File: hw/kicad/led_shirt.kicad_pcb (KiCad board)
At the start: 2 copper layers, 20.6 x 20.6 mm, 22 parts, among them J1 10103593-0001LF, P6 b+, P7 b-, Q1 MOS_N_np, SW1 SW_PUSH, U1 MCP73831, U2 PIC12F1822

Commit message: save some changes. need to switch to dual n-fet package.
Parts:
- removed P6: b+, noah_hole_1
- removed P7: b-, noah_hole_1
- removed med_test_hole (x2): VAL**, med_test_hole
- Q1: value MOS_N_np -> MOSFET_N
- R1: value 3.3kΩ -> 10kΩ
- R2: value 3.3kΩ -> 0Ω
- R3: value 10kΩ -> 10K
- R4: value 0Ω -> 10K
- R5, R6: value 10K -> 3.3kΩ
- U1: value MCP73831 -> PIC12F1822
- U2: value PIC12F1822 -> MCP73831
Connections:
- D1 pad 1: vbus -> vbat
- D1 pad 2: N-0000013 -> Net-(D1-Pad2)
- D2 pad 2: N-0000018 -> Net-(D1-Pad2)
- D3 pad 2: N-0000018 -> Net-(D1-Pad2)
- D4 pad 2: N-0000018 -> Net-(D1-Pad2)
- D5 pad 1: vbat -> vbus
- D5 pad 2: N-0000018 -> Net-(D5-Pad2)
- J1 pad 2: (no net) -> icspdat
- J1 pad 3: (no net) -> mclr
- J1 pad 4: (no net) -> icspclk
- Q1 pad 1: N-0000011 -> Net-(Q1-Pad1)
- Q1 pad 2: GND -> Net-(Q1-Pad2)
- Q1 pad 3: N-0000016 -> vbat
- R1 pad 1: N-0000013 -> Net-(Q1-Pad1)
- R1 pad 2: N-000001 -> GND
- R2 pad 1: N-0000014 -> Net-(D1-Pad2)
- R2 pad 2: GND -> Net-(Q2-Pad3)
- R3 pad 1: vbat -> mclr
- R3 pad 2: N-0000017 -> vbat
- R4 pad 1: N-0000018 -> Net-(Q2-Pad1)
- R4 pad 2: N-0000016 -> GND
- R5 pad 1: mclr -> Net-(R5-Pad1)
- R5 pad 2: vbat -> GND
- R6 pad 1: N-0000011 -> Net-(D5-Pad2)
- R6 pad 2: GND -> Net-(R6-Pad2)
- SW1 pad 1: GND -> vbat
- SW1 pad 2: N-0000017 -> Net-(Q1-Pad1)
- U1 pad 1: N-000001 -> Net-(Q1-Pad2)
- U1 pad 2: GND -> Net-(Q1-Pad1)
- U1 pad 3: vbat -> Net-(U1-Pad3)
- U1 pad 4: vbus -> mclr
- U1 pad 5: N-0000014 -> Net-(Q2-Pad1)
- U2 pad 1: vbat -> Net-(R6-Pad2)
- U2 pad 2: N-0000017 -> GND
- U2 pad 3: (no net) -> vbat
- U2 pad 4: mclr -> vbus
- U2 pad 5: N-0000011 -> Net-(R5-Pad1)
- U2 pad 8: GND -> (no net)
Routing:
- net N-0000018: track 35.3 -> 0.00 mm, vias 2 -> 0
- net Net-(D1-Pad2): track 0.00 -> 33.4 mm
- net Net-(R6-Pad2): track 0.00 -> 13.6 mm
- net GND: track 15.3 -> 6.56 mm
- net N-0000011: track 7.94 -> 0.00 mm, vias 2 -> 0
- net Net-(Q2-Pad1): track 0.00 -> 7.67 mm, vias 0 -> 2
- net vbat: track 49.1 -> 42.5 mm, vias 1 -> 2
- net Net-(Q1-Pad1): track 0.00 -> 6.28 mm, vias 0 -> 1
- net vbus: track 13.0 -> 8.07 mm
- net N-0000017: track 4.94 -> 0.00 mm, vias 1 -> 0
- net mclr: track 3.55 -> 7.89 mm, vias 1 -> 0
- net Net-(R5-Pad1): track 0.00 -> 4.07 mm, vias 0 -> 3
- net (no net): track 0.00 -> 3.20 mm
- net N-0000013: track 3.15 -> 0.00 mm
- net Net-(U1-Pad3): track 0.00 -> 2.98 mm
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
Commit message: update sch
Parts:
- added P1: b+, noah:noah_hole_1, F.Cu at (153.7, 117.0)
- added P2: b-, kicadlib:med_test_hole, F.Cu at (153.7, 117.0)
- C1, C2, R1, R2, R3, R4, R5, R6: footprint SM0603 -> kicadlib:SMD_0603_R
- D1: footprint SM0603 -> kicadlib:plcc2
- D2, D3, D4, D5: footprint plcc2 -> kicadlib:plcc2
- J1: footprint 10118193-0001LF -> kicadlib:usb_micro_b_smt
- Q1: value MOSFET_N -> PN_MOSFET_DUAL; footprint SOT23 -> kicadlib:SMD_SOT23-6
- SW1: footprint SW_PB_4PIN_SMT_real -> noah:SW_PB_4PIN_SMT_real
- U1: footprint MCP73831 -> noah:PIC12F1822-SOIC-8
- U2: footprint PIC12F1822-SOIC-8 -> kicadlib:MCP73831
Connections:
- net Net-(Q1-Pad2) renamed Q2_S
- Q1 pad 1: Net-(Q1-Pad1) -> Q1_G
- Q1 pad 3: vbat -> Q2_G
- R1 pad 1: Net-(Q1-Pad1) -> vbat
- R1 pad 2: GND -> Q2_G
- R2 pad 2: Net-(Q2-Pad3) -> Q1_D
- R4 pad 1: Net-(Q2-Pad1) -> Q1_G
- SW1 pad 1: vbat -> GND
- SW1 pad 2: Net-(Q1-Pad1) -> Q2_G
- U1 pad 2: Net-(Q1-Pad1) -> Q2_G
- U1 pad 5: Net-(Q2-Pad1) -> Q1_G
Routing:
- net GND: track 6.56 -> 18.7 mm, vias 2 -> 1
- net vbat: track 42.5 -> 31.2 mm, vias 2 -> 1
- net (no net): track 3.20 -> 13.3 mm, vias 0 -> 3
- net Net-(Q2-Pad1): track 7.67 -> 0.00 mm, vias 2 -> 0
- net Net-(D1-Pad2): track 33.4 -> 40.9 mm, vias 0 -> 2
- net mclr: track 7.89 -> 1.46 mm, vias 0 -> 1
- net Net-(Q1-Pad1): track 6.28 -> 0.00 mm, vias 1 -> 0
- net Q1_G: track 0.00 -> 5.99 mm, vias 0 -> 1
- net Net-(R6-Pad2): track 13.6 -> 18.5 mm
- net Net-(R5-Pad1): track 4.07 -> 0.95 mm, vias 3 -> 1
- net Net-(U1-Pad3): track 2.98 -> 0.00 mm
- net vbus: track 8.07 -> 5.14 mm
- net Net-(D5-Pad2): track 2.47 -> 0.00 mm
- net Q2_G: track 0.00 -> 1.36 mm
- net Q2_S: track 1.80 -> 2.81 mm

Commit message: more components
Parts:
- removed D1, D3, D4, D5: LED, kicadlib:plcc2
- removed P1: b+, noah:noah_hole_1
- removed P2: b-, kicadlib:med_test_hole
- added C3: 4.7µF, kicadlib:SMD_0603_R, F.Cu at (163.8, 118.1)
- added J4: 5_PIN_HDR, kicadlib:SMD_JST_5_PIN_VERT, F.Cu at (137.2, 101.6)
- added R10: 3.3kΩ, kicadlib:SMD_0603_R, F.Cu at (153.7, 119.4)
- added R7: 10K, kicadlib:SMD_0603_R, F.Cu at (152.4, 109.2)
- added R8: 10K, kicadlib:SMD_0603_R, F.Cu at (146.1, 108.0)
- added R9: 3.3kΩ, kicadlib:SMD_0603_R, F.Cu at (171.4, 116.8)
- added U3: MCP73831, kicadlib:SMD_SOT23-5, F.Cu at (146.1, 99.1)
- C1: value 4.7µF -> 1.0µF; moved to F.Cu
- C2, J1, R1: moved to F.Cu
- D2: footprint kicadlib:plcc2 -> kicadlib:SMD_0603_LED
- R2: value 0Ω -> 10kΩ; moved to F.Cu
- R3, R4: value 10K -> 10kΩ; moved to F.Cu
- R5: value 3.3kΩ -> 0Ω
- R6: value 3.3kΩ -> 10kΩ
- SW1: footprint noah:SW_PB_4PIN_SMT_real -> kicadlib:spst_pushbutton_smd
- U1: value PIC12F1822 -> AP3012; footprint noah:PIC12F1822-SOIC-8 -> kicadlib:SMD_SOT23-5; moved to F.Cu
- U2: value MCP73831 -> PIC12F1822; footprint kicadlib:MCP73831 -> kicadlib:SMD_SOIC-8; moved to F.Cu
- moved C1 23.0 mm to (161.3, 111.8), turned to 0 degrees
- moved SW1 22.5 mm to (138.4, 113.0)
- moved Q1 19.1 mm to (154.9, 114.3)
- moved J1 18.5 mm to (135.9, 110.5), turned to 0 degrees
- moved U2 14.9 mm to (165.1, 106.7), turned to 0 degrees
- moved R2 14.1 mm to (143.5, 104.1), turned to 0 degrees
- moved R6 13.9 mm to (151.1, 114.3), turned to 0 degrees
- moved C2 13.0 mm to (147.3, 104.1), turned to 0 degrees
- moved R1 11.9 mm to (154.9, 102.9), turned to 0 degrees
- moved U1 7.74 mm to (160.0, 99.1), turned to 0 degrees
- moved R4 7.38 mm to (158.8, 104.1), turned to 0 degrees
- moved D2 5.46 mm to (156.2, 106.7), turned to 0 degrees
- moved R3 3.97 mm to (151.1, 105.4), turned to 0 degrees
- moved R5 3.06 mm to (152.4, 97.8), turned to 0 degrees
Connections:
- C1 pad 1: vbus -> /+12v
- C2 pad 1: vbat -> /vbus
- D2 pad 1: vbat -> /vbus
- D2 pad 2: Net-(D1-Pad2) -> Net-(D2-Pad2)
- J1 pad 1: vbus -> /vbus
- J1 pad 2: icspdat -> Net-(J1-Pad2)
- J1 pad 3: mclr -> Net-(J1-Pad3)
- J1 pad 4: icspclk -> Net-(J1-Pad4)
- Q1 pad 1: Q1_G -> /led_cntrl
- Q1 pad 2: Q2_S -> /lps
- Q1 pad 3: Q2_G -> /~lps_enable
- Q1 pad 4: vbat -> /vbat
- Q1 pad 6: Q1_D -> Net-(Q1-Pad6)
- R1 pad 1: vbat -> /+12v
- R1 pad 2: Q2_G -> Net-(R1-Pad2)
- R2 pad 1: Net-(D1-Pad2) -> Net-(R1-Pad2)
- R2 pad 2: Q1_D -> GND
- R3 pad 1: mclr -> /vbat
- R3 pad 2: vbat -> /~lps_enable
- R4 pad 1: Q1_G -> /lps
- R4 pad 2: GND -> /batt_sns
- R5 pad 1: Net-(R5-Pad1) -> /led-
- R5 pad 2: GND -> Net-(Q1-Pad6)
- R6 pad 1: Net-(D5-Pad2) -> /batt_sns
- R6 pad 2: Net-(R6-Pad2) -> GND
- SW1 pad 2: Q2_G -> /~lps_enable
- U1 pad 1: Q2_S -> Net-(D1-Pad2)
- U1 pad 2: Q2_G -> GND
- U1 pad 3: Net-(U1-Pad3) -> Net-(R1-Pad2)
- U1 pad 4: mclr -> /lps
- U1 pad 5: Q1_G -> /vbat
- U2 pad 1: Net-(R6-Pad2) -> /lps
- U2 pad 2: GND -> /~lps_enable
- U2 pad 3: vbat -> /batt_sns
- U2 pad 4: vbus -> /mclr
- U2 pad 5: Net-(R5-Pad1) -> /led_cntrl
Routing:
- net Net-(D1-Pad2): track 40.9 -> 0.00 mm, vias 2 -> 0
- net vbat: track 31.2 -> 0.00 mm, vias 1 -> 0
- net GND: track 18.7 -> 0.00 mm, vias 1 -> 0
- net Net-(R6-Pad2): track 18.5 -> 0.00 mm
- net (no net): track 13.3 -> 0.00 mm, vias 3 -> 0
- net Q1_G: track 5.99 -> 0.00 mm, vias 1 -> 0
- net vbus: track 5.14 -> 0.00 mm
- net Q2_S: track 2.81 -> 0.00 mm
- net mclr: track 1.46 -> 0.00 mm, vias 1 -> 0
- net Q2_G: track 1.36 -> 0.00 mm
- net Net-(R5-Pad1): track 0.95 -> 0.00 mm, vias 1 -> 0
- removed copper zone on B.Cu, net GND
- removed copper zone on F.Cu, net GND
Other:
- board outline removed
- board text removed: "+"
- board text removed: "-"
- board text removed: "c"
- board text removed: "d"
- board text removed: "git.io/FEFjUw v2.0"
- board text removed: "ledshirt"
- board text removed: "m"

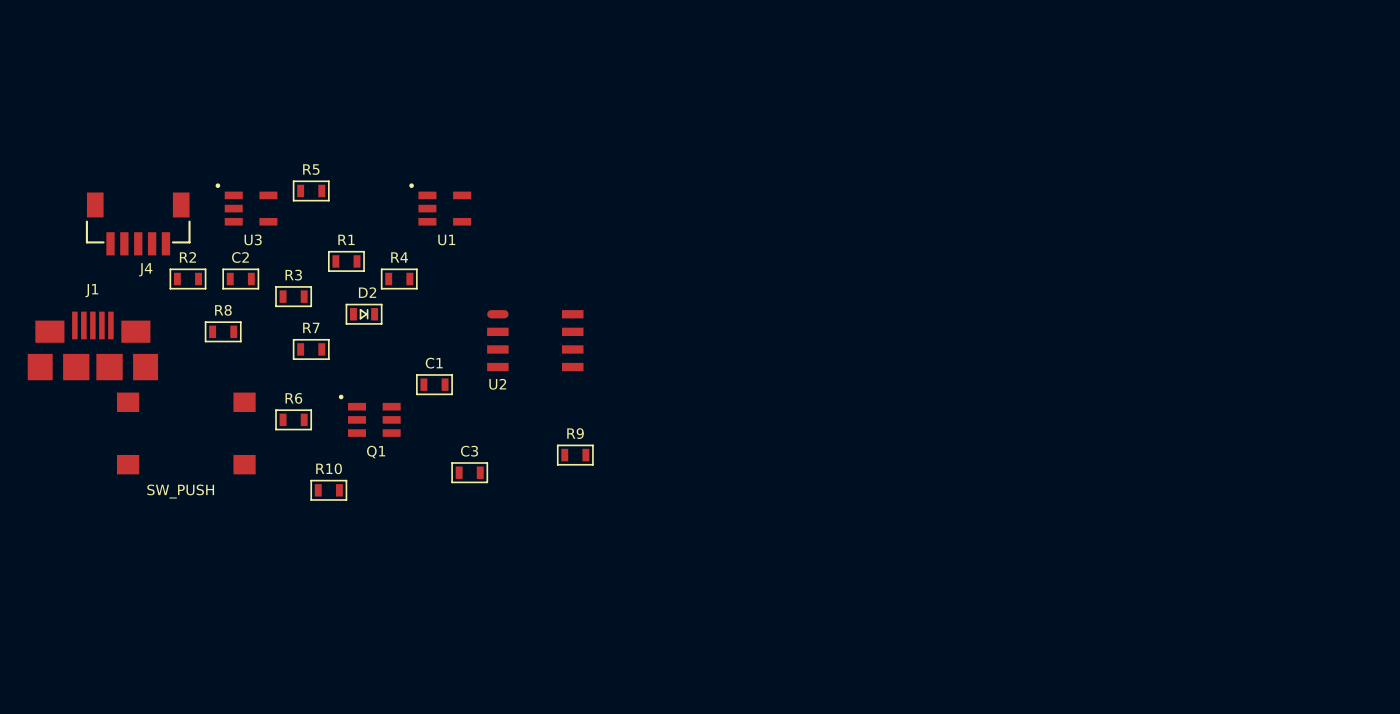
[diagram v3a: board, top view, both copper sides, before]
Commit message: footprints mostly done, some missing modules
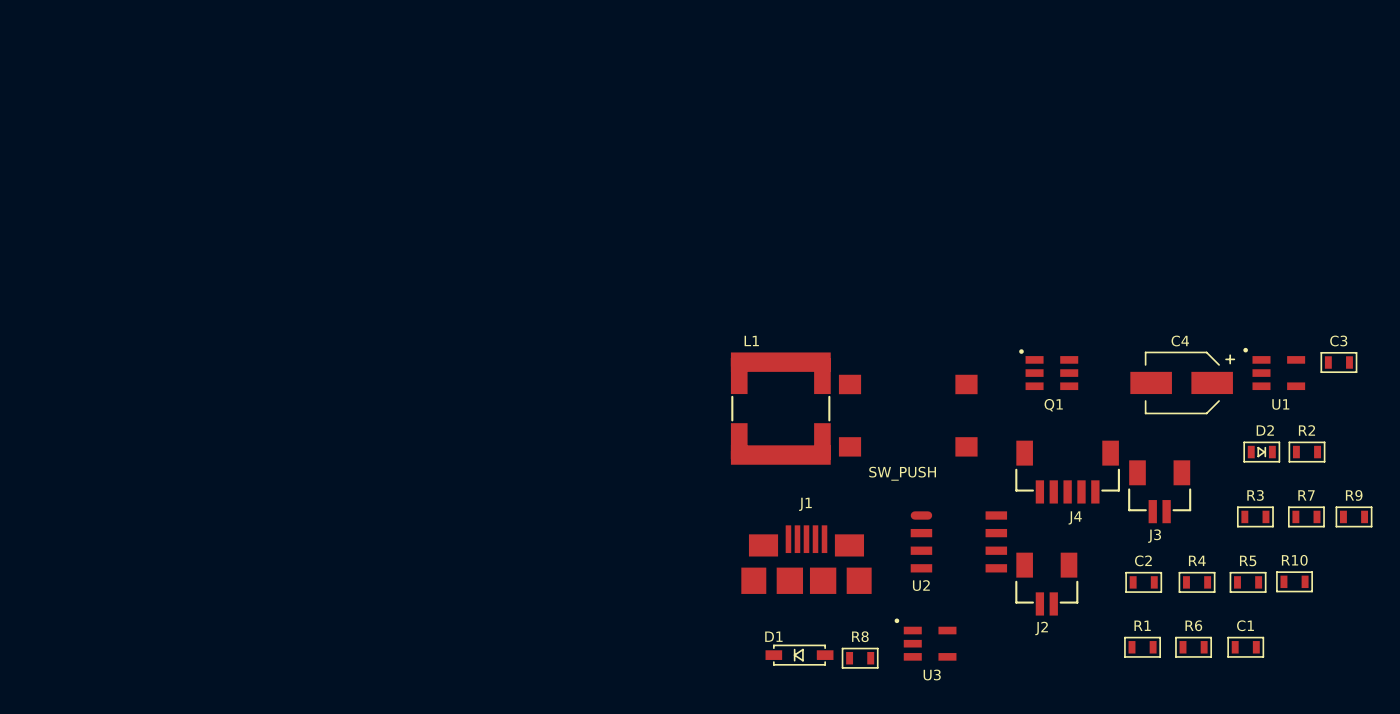
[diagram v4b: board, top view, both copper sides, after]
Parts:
- added C4: CP1, kicadlib:SMD_5X5.2_CAP, F.Cu at (212.2, 111.6)
- added D1: D_Schottky, kicadlib:SMD_SOD-123_DIODE, F.Cu at (185.0, 131.3)
- added J2: 2_PIN_HDR, kicadlib:SMD_JST_2_PIN_VERT, F.Cu at (204.2, 127.6)
- added J3: 2_PIN_HDR, kicadlib:SMD_JST_2_PIN_VERT, F.Cu at (212.3, 120.9)
- added L1: INDUCTOR, kicadlib:SMD_IND_6.8x6.8_SRR6038-100Y, F.Cu at (185.5, 111.1)
- moved R2 81.7 mm to (224.2, 116.6)
- moved R5 73.2 mm to (220.0, 126.0)
- moved R7 72.8 mm to (224.2, 121.3)
- moved R3 71.2 mm to (220.5, 121.3)
- moved R10 70.0 mm to (223.3, 126.0)
- moved J4 69.4 mm to (204.2, 119.5)
- moved C2 68.7 mm to (212.4, 126.0)
- moved R6 67.0 mm to (216.0, 130.7)
- moved D2 65.5 mm to (221.0, 116.6)
- moved R1 63.8 mm to (212.4, 130.7)
- moved C3 63.2 mm to (226.5, 110.2)
- moved R4 61.6 mm to (216.3, 126.0)
- moved C1 61.5 mm to (219.8, 130.7)
- moved U1 61.3 mm to (220.2, 110.9)
- moved U3 58.2 mm to (195.0, 130.4)
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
